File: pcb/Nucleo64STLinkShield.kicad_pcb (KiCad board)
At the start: 4 copper layers, 44 x 24.6 mm, 13 parts, among them J1 SWD, J2 Debug, J3 UART, J4 USB Power, J5 Nucleo-64 ST-Link Selector, J6 Conn_01x06, J7 Conn_01x06, SW2 B3U-1000P

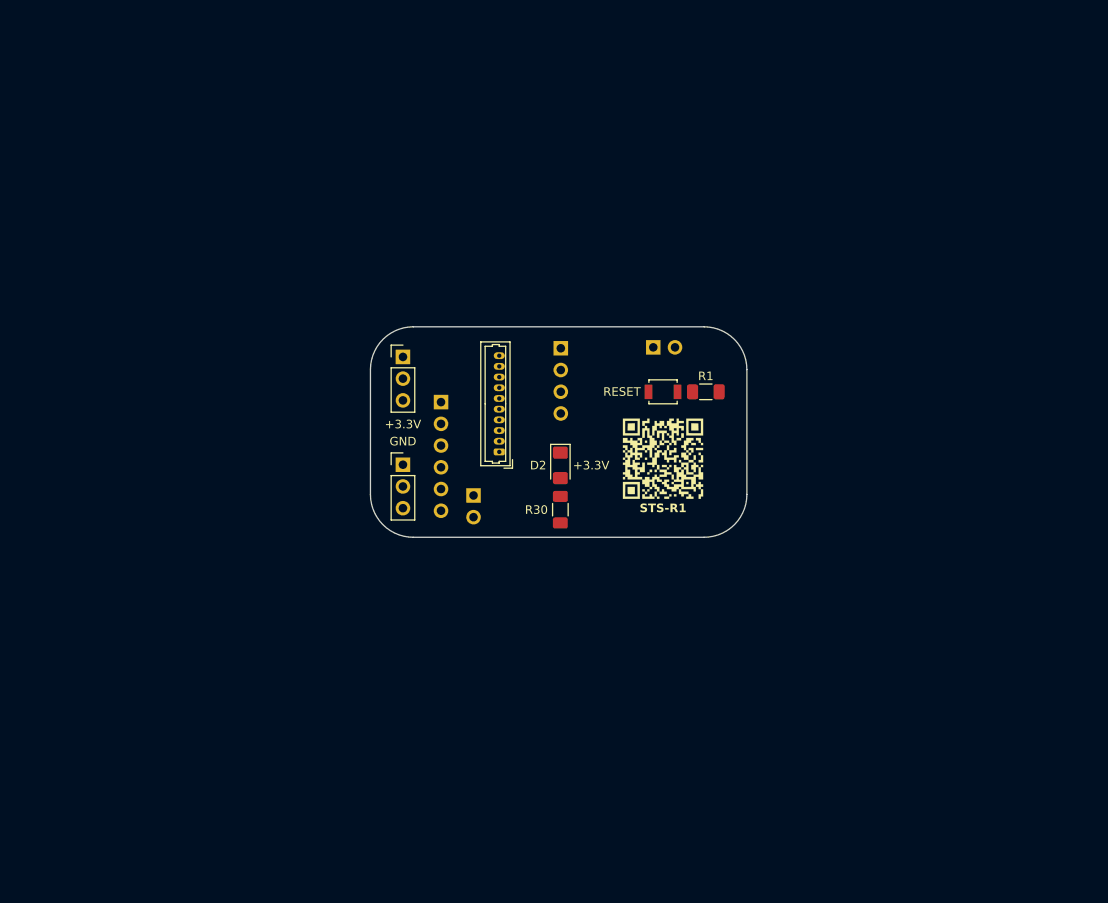
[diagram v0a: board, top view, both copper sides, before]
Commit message: Routed the ST-Link shield.
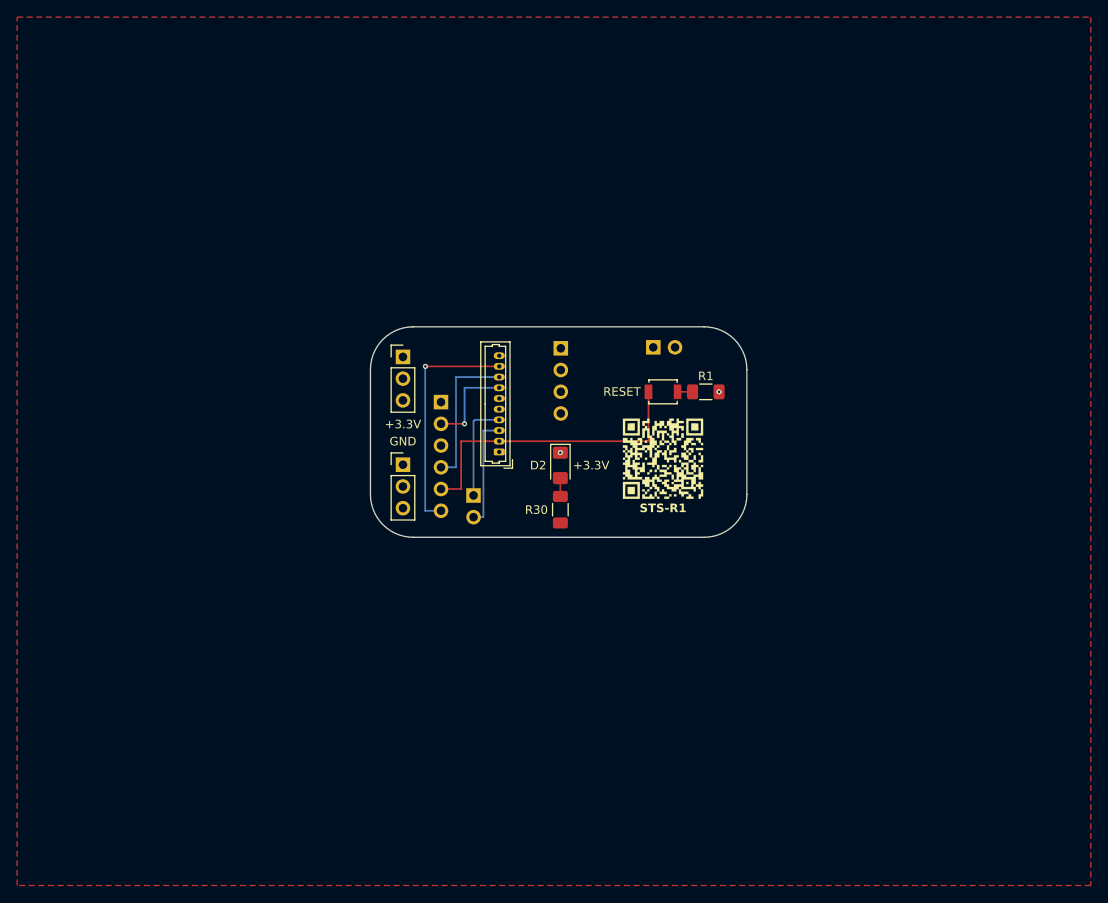
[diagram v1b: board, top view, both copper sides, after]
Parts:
- J6, J7: value Conn_01x06 -> Conn_01x03
- turned SW2 to 180 degrees
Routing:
- net RESET: track 0.00 -> 35.6 mm
- net swo: track 0.00 -> 27.4 mm, vias 0 -> 1
- net swdio: track 0.00 -> 17.4 mm
- net stlink_tx: track 0.00 -> 13.1 mm
- net stlink_rx: track 0.00 -> 11.8 mm
- net swclk: track 0.00 -> 11.0 mm, vias 0 -> 1
- net /VDD_LED_ANODE: track 0.00 -> 2.14 mm
- net /RESET_PRESSED: track 0.00 -> 1.75 mm
- net GND: vias 0 -> 2
- added copper zone on F.Cu, net +3.3V
- added copper zone on In1.Cu, net GND
- added copper zone on In2.Cu, net GND
